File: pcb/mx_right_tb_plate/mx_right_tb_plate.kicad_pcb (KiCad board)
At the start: 2 copper layers, 139.8 x 113.1 mm, 0 parts

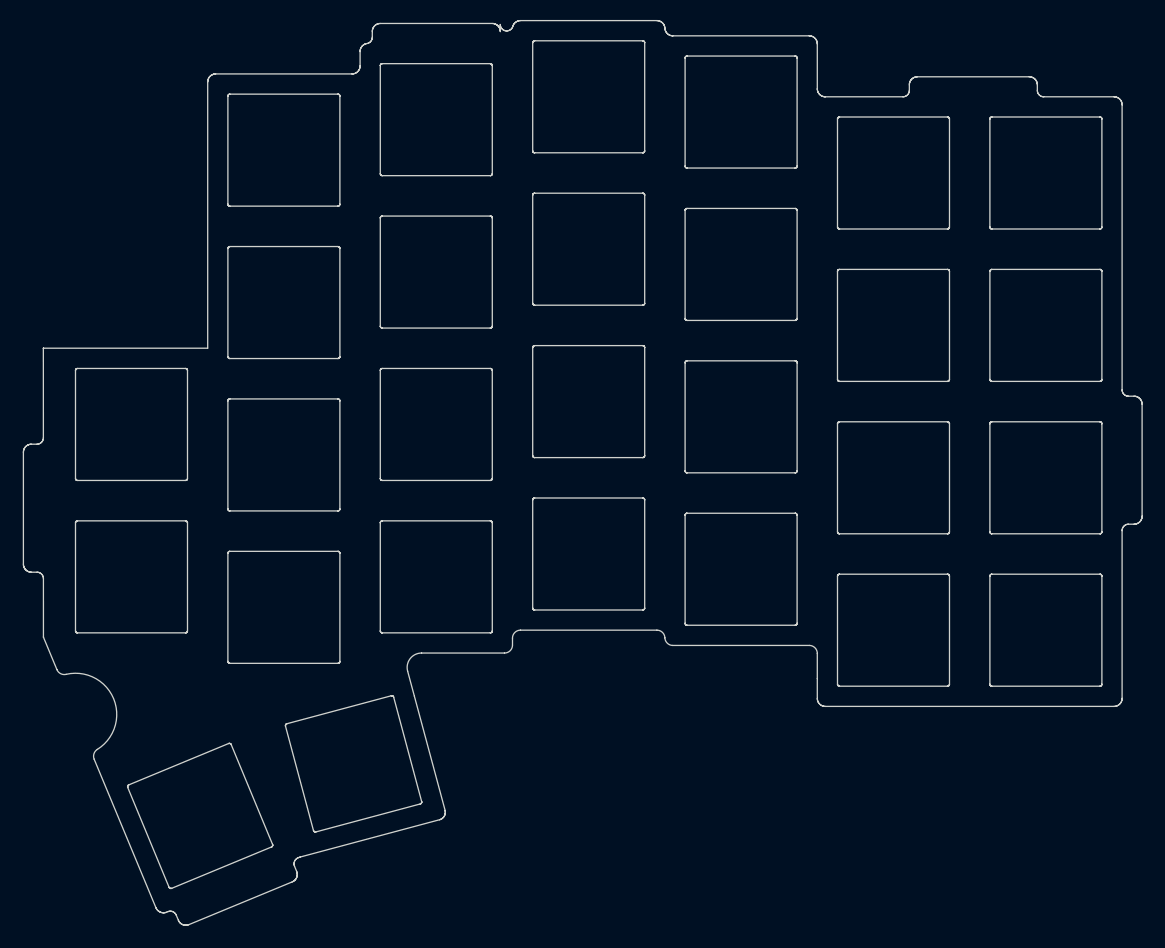
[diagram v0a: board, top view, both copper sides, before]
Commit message: feat: order-ready MX boards (phi 5 centre holes), separate left / right plates, case updates
- PCBs: switch centre holes phi 4.1 -> 5 for Kailh Choc v2 (centre_hole.py); the tracks that fell
  inside the new hole clearance are rerouted by centre_reroute.py (grid A*, vias where one layer is
  full). DRC errors unchanged, 0 unconnected, schematic parity as before.
- SW32 stays a 3-pin THT footprint (2.54 mm); the case's knob opening follows its middle pin
  (SW_Y -54.86) and the finger scoop sits 1 mm toward +y to avoid a thin wall at the MCU block.
- Plates: one per side (pcb/mx_left_plate, pcb/mx_right_tb_plate) instead of the shared
  breakaway plate; 1.2 mm 3MFs for test prints.
- Top case: chamfer on the top outer edge (top_chamfer); machinability probe fix.
- Regenerated specs, 3MFs and MCU cover DXFs; all four documents pass check.py,
  check_parts.py and machinability.py.

Co-Authored-By: Claude Opus 5.5 <noreply@anthropic.com>
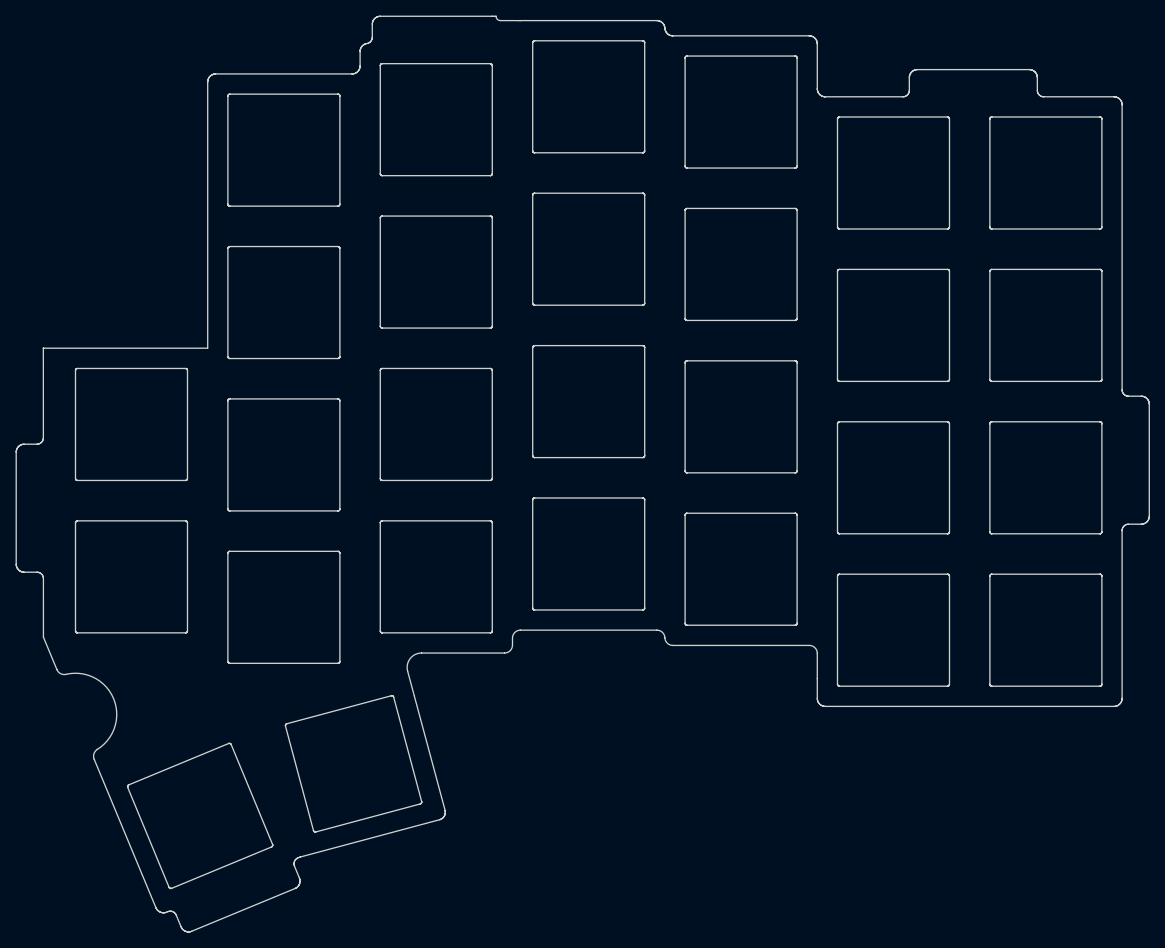
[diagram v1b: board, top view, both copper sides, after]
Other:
- board size 139.8 x 113.1 mm -> 141.6 x 114.5 mm
